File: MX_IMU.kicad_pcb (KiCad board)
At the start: 4 copper layers, 40 x 36 mm, 53 parts, among them J1 CAN, J2 USART, J3 2171750001, J401 SWD, SW1 SW_SPST, U1 ld39150dt33-r, U2 ICM-42688-P, U200 STM32F405RGT6, U4 AT24C256, U6 TJA1051T/3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

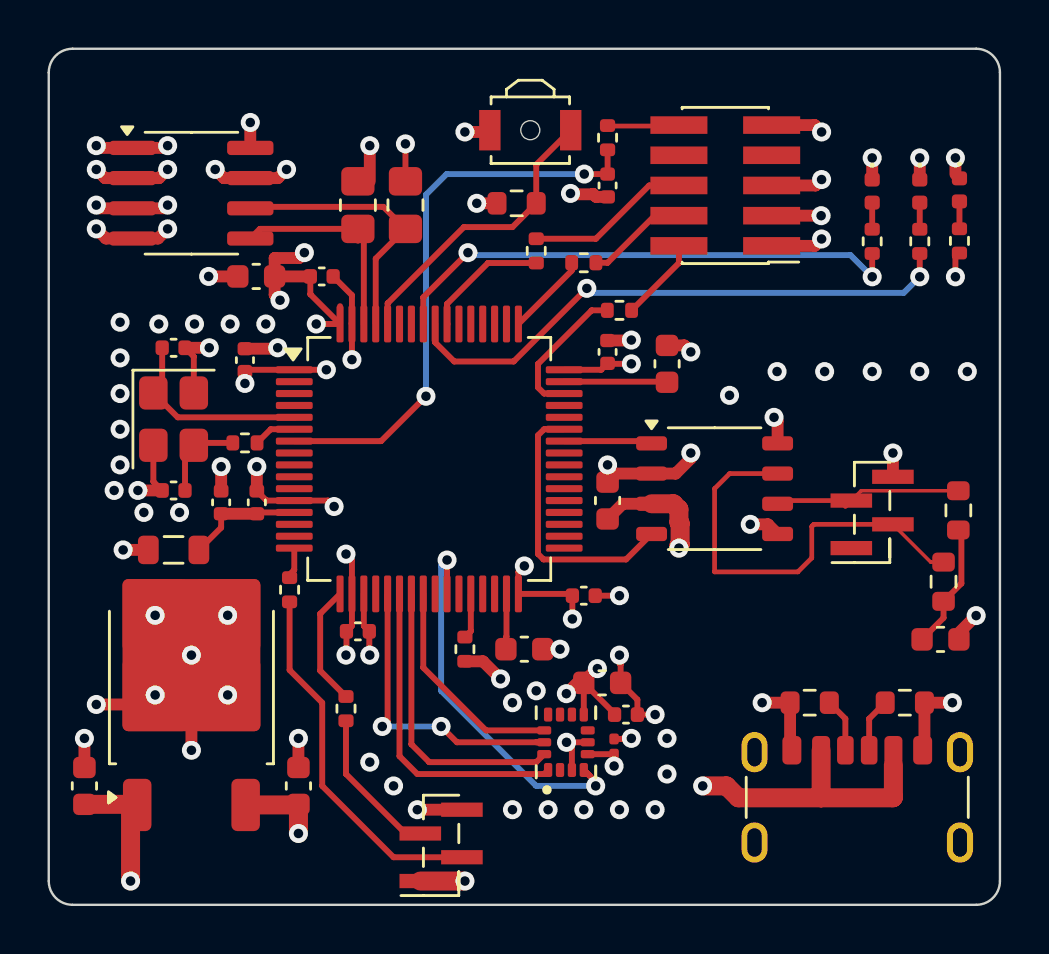
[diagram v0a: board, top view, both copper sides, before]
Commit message: add mounting hole
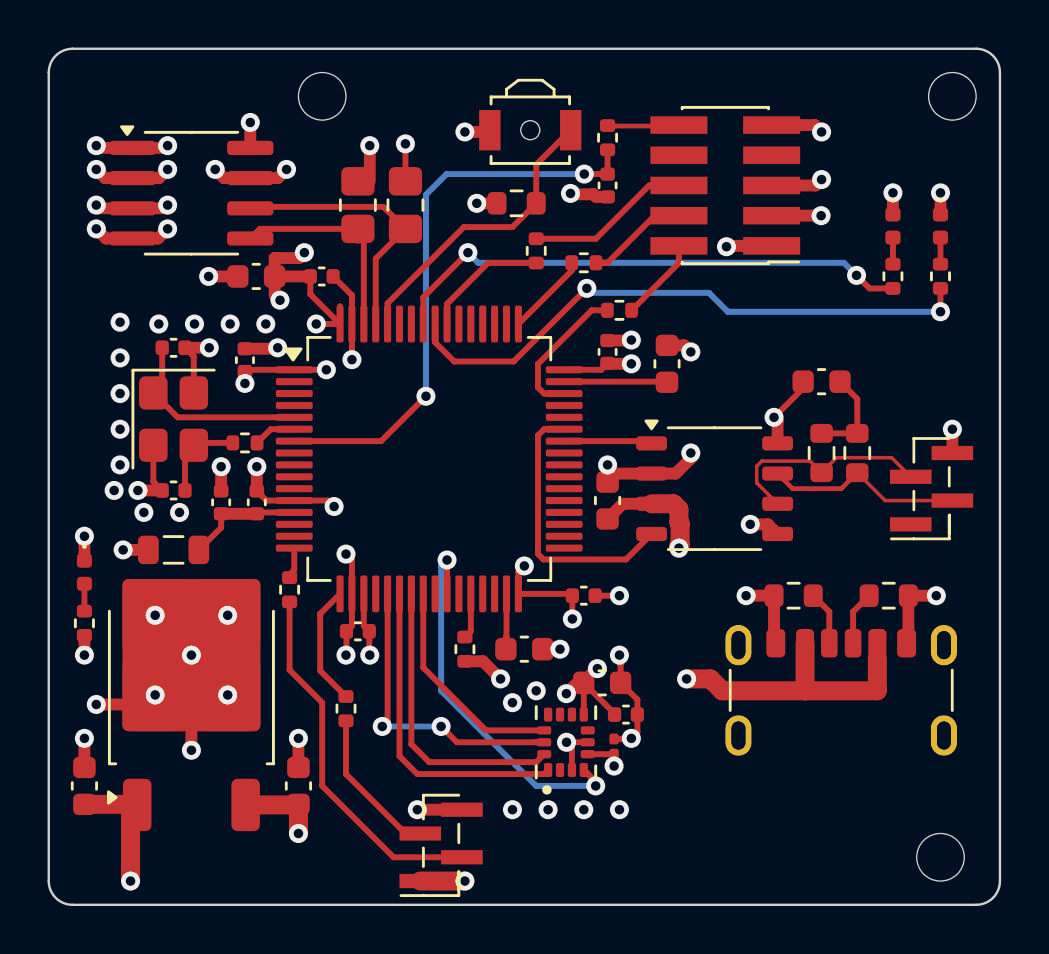
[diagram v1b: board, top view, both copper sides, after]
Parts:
- added ?: , , F.Cu at (160.1, 88.3)
- added REF**: MountingHole_2mm, MountingHole:MountingHole_2mm, F.Cu at (159.6, 120.3)
- added REF**: MountingHole_2mm, MountingHole:MountingHole_2mm, F.Cu at (133.6, 88.3)
- moved D5 40.2 mm to (123.6, 108.3)
- moved R29 40.2 mm to (123.6, 110.5)
- moved C31 11.9 mm to (154.6, 100.3), turned to 180 degrees
- moved R20 6.52 mm to (156.1, 103.3), turned to 90 degrees
- moved R19 6.24 mm to (154.6, 103.3), turned to 90 degrees
- moved J3 4.55 mm to (155.4, 114.4)
- moved R1 4.55 mm to (157.4, 109.3)
- moved R2 4.55 mm to (153.4, 109.3)
- moved J1 2.69 mm to (159.2, 104.8)
- moved D3 1.71 mm to (159.6, 93.8)
- moved D4 1.71 mm to (157.6, 93.8)
- moved R13 1.71 mm to (159.6, 95.9)
- moved R14 1.71 mm to (157.6, 95.9)
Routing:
- net /Connectors/CAN1+: track 18.3 -> 8.71 mm
- net Net-(C31-Pad1): track 5.34 -> 3.98 mm
- net /Connectors/CAN1-: track 8.18 -> 9.49 mm
- net GND: track 90.6 -> 91.7 mm, vias 54 -> 52
- net STATUS_LED1: track 24.1 -> 25.0 mm
- net +3.3V: track 44.8 -> 44.3 mm
- net (no net): vias 29 -> 18

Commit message: update
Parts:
- removed ?: , 
- removed C29: 100n, Capacitor_SMD:C_0603_1608Metric
- removed C7: 2u2, Capacitor_SMD:C_0603_1608Metric
- removed REF** (x2): MountingHole_2mm, MountingHole:MountingHole_2mm
- added C2: 100n, Capacitor_SMD:C_0402_1005Metric, F.Cu at (145.6, 105.3)
- added C5: 2u2, Capacitor_SMD:C_0603_1608Metric, F.Cu at (132.6, 117.3)
- moved C4 13.5 mm to (145.3, 113.0), turned to 0 degrees
- moved J3 4.21 mm to (155.6, 118.6)
- moved R1 4.21 mm to (157.6, 113.5)
- moved R2 4.21 mm to (153.6, 113.5)
- moved R29 2.32 mm to (123.6, 108.2), turned to -90 degrees
- moved D5 1.97 mm to (123.6, 110.3), turned to 90 degrees
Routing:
- net GND: track 91.7 -> 90.0 mm
- net EEPROM_SDA: track 9.88 -> 8.44 mm
- net Net-(J401-Pin_4): track 4.31 -> 3.29 mm
- net Net-(C211-Pad1): track 3.73 -> 3.07 mm
- net Net-(J2-Pin_3): track 6.40 -> 5.78 mm
- net HSE_IN: track 8.40 -> 7.88 mm

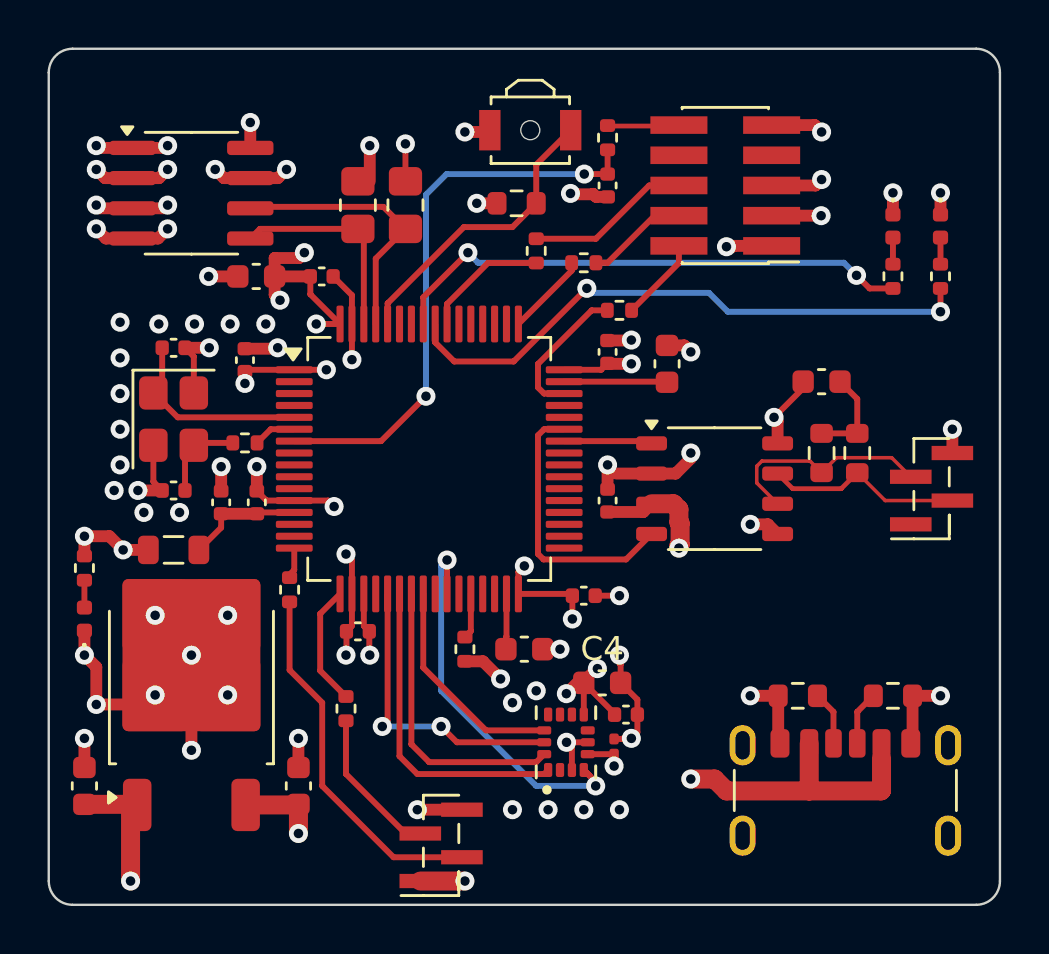
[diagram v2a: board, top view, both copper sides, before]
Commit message: add mountinghole in sch
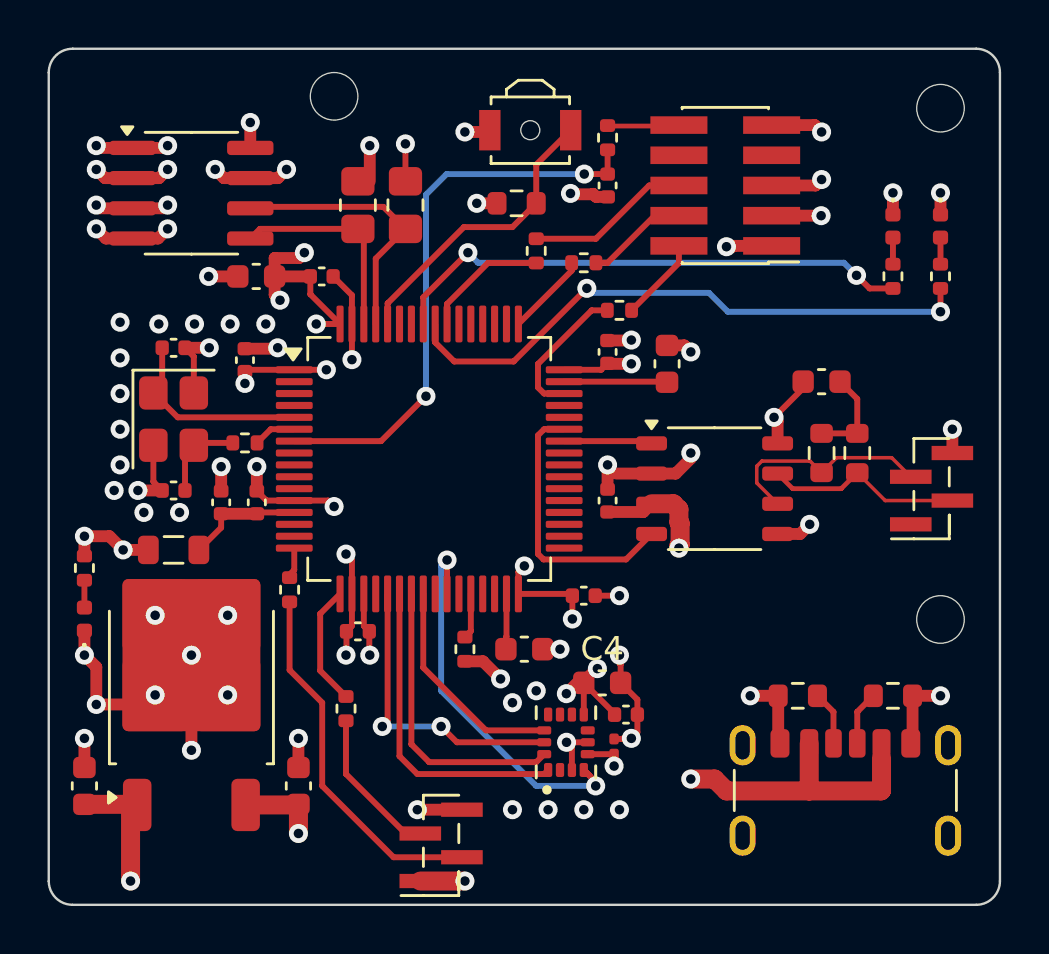
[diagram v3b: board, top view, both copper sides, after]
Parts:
- added H1: MountingHole, MountingHole:MountingHole_2mm, F.Cu at (159.6, 88.8)
- added H2: MountingHole, MountingHole:MountingHole_2mm, F.Cu at (134.1, 88.3)
- added H3: MountingHole, MountingHole:MountingHole_2mm, F.Cu at (159.6, 110.3)

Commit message: update bom
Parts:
- J1: value CAN -> pinheader; footprint Connector_PinHeader_1.00mm:PinHeader_1x04_P1.00mm_Vertical_SMD_Pin1Right -> Connector_PinHeader_1.27mm:PinHeader_1x04_P1.27mm_Vertical
- J2: value USART -> pinheader; footprint Connector_PinHeader_1.00mm:PinHeader_1x04_P1.00mm_Vertical_SMD_Pin1Right -> Connector_PinHeader_1.27mm:PinHeader_1x04_P1.27mm_Vertical
- J401: footprint Connector_PinHeader_1.27mm:PinHeader_2x05_P1.27mm_Vertical_SMD -> Connector_PinHeader_1.27mm:PinHeader_2x05_P1.27mm_Vertical
- R19, R20: footprint Resistor_SMD:R_0603_1608Metric -> Resistor_SMD:R_0402_1005Metric
- moved D3 4.25 mm to (155.6, 92.3)
- moved D4 4.25 mm to (153.6, 92.3)
- moved R13 4.25 mm to (155.6, 94.5)
- moved R14 4.25 mm to (153.6, 94.5)
- moved J2 2.87 mm to (136.1, 121.2)
- moved J401 2.65 mm to (149.8, 94.6)
- moved J1 2.10 mm to (160.1, 106.7)
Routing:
- net STATUS_LED2: track 22.3 -> 17.6 mm
- net STATUS_LED1: track 25.0 -> 20.8 mm
- net Net-(J2-Pin_2): track 15.4 -> 12.0 mm
- net GND: track 90.0 -> 87.8 mm
- net /Connectors/CAN1-: track 9.30 -> 10.9 mm
- net +3.3V: track 44.0 -> 42.8 mm
- net Net-(J2-Pin_3): track 5.78 -> 4.73 mm
- net Net-(J401-Pin_4): track 3.29 -> 4.32 mm
- net /Connectors/CAN1+: track 8.38 -> 8.88 mm
